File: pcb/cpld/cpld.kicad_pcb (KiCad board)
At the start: 4 copper layers, 104.4 x 82.7 mm, 30 parts, among them J1 Micro_SD_Card_Det1, J2 Bus_ISA_8bit_AB_Rev0, J3 Atmel-JTAG-10, SW1 ADDR SEL, U1 ATF1504AS-xJx44, U2 AMS1117-3.3, U3 74LVC125, U4 74HCT688, X1 16MHz

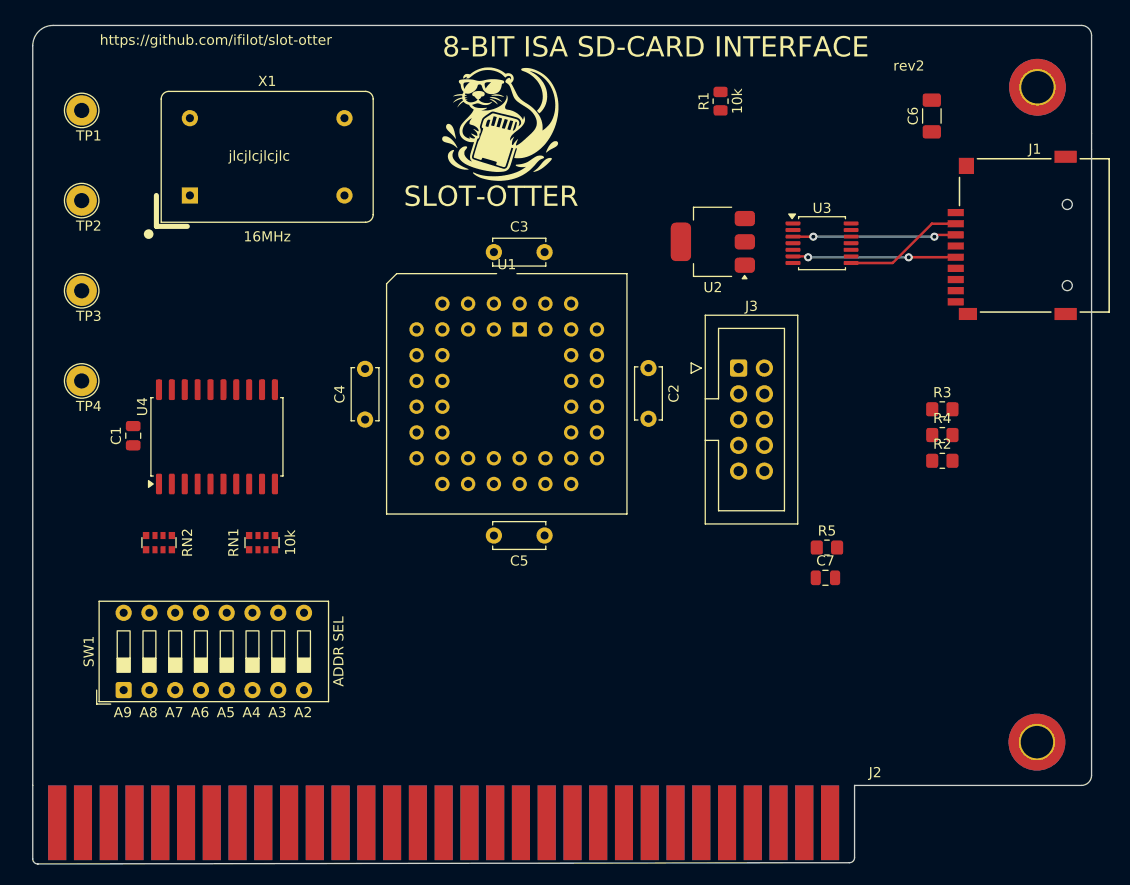
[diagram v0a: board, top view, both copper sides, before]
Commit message: Refactoring otternav and initial commit copying from HD to SD
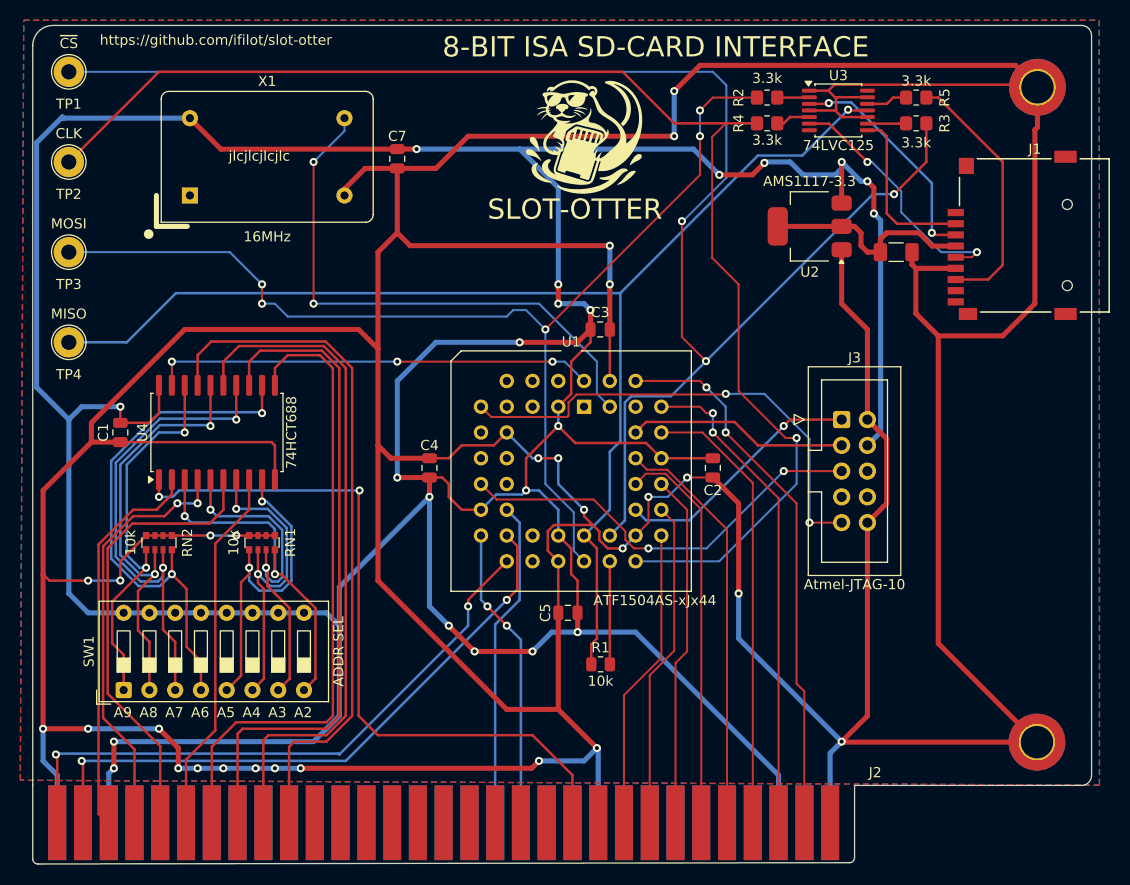
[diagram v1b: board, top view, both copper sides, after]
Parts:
- C2, C3, C4, C5: footprint Capacitor_THT:C_Disc_D5.0mm_W2.5mm_P5.00mm -> Capacitor_SMD:C_0805_2012Metric
- moved C7 59.1 mm to (112.6, 50.7), turned to -90 degrees
- moved R1 56.8 mm to (132.7, 100.6), turned to 0 degrees
- moved R5 45.2 mm to (163.8, 44.7), turned to 180 degrees
- moved R2 39.8 mm to (149.1, 44.7)
- moved R4 35.3 mm to (149.1, 47.2)
- moved R3 28.3 mm to (163.8, 47.2), turned to 180 degrees
- moved C6 13.9 mm to (161.8, 59.9), turned to 0 degrees
- moved U3 13.2 mm to (156.1, 46.0)
- moved C3 13.0 mm to (132.6, 67.5)
- moved C2 11.7 mm to (143.7, 81.2)
- moved J3 11.4 mm to (156.4, 76.4)
- moved U1 9.92 mm to (131.0, 75.2)
- moved U2 9.67 mm to (153.3, 57.4)
- moved G*** 8.35 mm to (131.0, 48.5)
- moved C5 7.96 mm to (129.5, 95.5)
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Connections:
- SW1 pad 5: Net-(RN1A-R1.2) -> Net-(RN1D-R4.2)
- SW1 pad 6: Net-(RN1B-R2.2) -> Net-(RN1C-R3.2)
- SW1 pad 7: Net-(RN1C-R3.2) -> Net-(RN1B-R2.2)
- SW1 pad 8: Net-(RN1D-R4.2) -> Net-(RN1A-R1.2)
- U1 pad 11: DB5 -> unconnected-(U1-I/O/PD1-Pad11)
- U1 pad 12: DB6 -> unconnected-(U1-I/O-Pad12)
- U1 pad 14: DB7 -> unconnected-(U1-I/O-Pad14)
- U1 pad 15: +5V -> VCC
- U1 pad 23: +5V -> VCC
- U1 pad 29: unconnected-(U1-I/O-Pad29) -> DB0
- U1 pad 3: +5V -> VCC
- U1 pad 31: unconnected-(U1-I/O-Pad31) -> DB1
- U1 pad 33: unconnected-(U1-I/O-Pad33) -> DB2
- U1 pad 34: unconnected-(U1-I/O-Pad34) -> DB3
- U1 pad 35: +5V -> VCC
- U1 pad 36: unconnected-(U1-I/O-Pad36) -> DB4
- U1 pad 37: unconnected-(U1-I/O-Pad37) -> DB5
- U1 pad 39: unconnected-(U1-I/O-Pad39) -> DB6
- U1 pad 4: DB0 -> unconnected-(U1-I/O-Pad4)
- U1 pad 40: unconnected-(U1-I/O-Pad40) -> DB7
- U1 pad 5: DB1 -> unconnected-(U1-I/O-Pad5)
- U1 pad 6: DB2 -> unconnected-(U1-I/O-Pad6)
- U1 pad 8: DB3 -> unconnected-(U1-I/O-Pad8)
- U1 pad 9: DB4 -> unconnected-(U1-I/O-Pad9)
- U4 pad 3: Net-(RN1D-R4.2) -> Net-(RN1A-R1.2)
- U4 pad 5: Net-(RN1C-R3.2) -> Net-(RN1B-R2.2)
- U4 pad 7: Net-(RN1B-R2.2) -> Net-(RN1C-R3.2)
- U4 pad 9: Net-(RN1A-R1.2) -> Net-(RN1D-R4.2)
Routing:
- net GND: track 0.00 -> 674.7 mm, vias 0 -> 27
- net VCC: track 0.00 -> 444.7 mm, vias 0 -> 21
- net ~{CS}: track 0.00 -> 152.5 mm, vias 0 -> 3
- net CLK: track 0.00 -> 132.9 mm, vias 0 -> 1
- net MISO: track 0.00 -> 127.1 mm, vias 0 -> 1
- net MOSI: track 0.00 -> 110.3 mm, vias 0 -> 5
- net AEN: track 0.00 -> 72.3 mm, vias 0 -> 2
- net A9: track 0.00 -> 69.3 mm
- net A8: track 0.00 -> 67.6 mm
- net A7: track 0.00 -> 66.3 mm
- net A6: track 0.00 -> 63.6 mm
- net A1: track 0.00 -> 62.0 mm, vias 0 -> 2
- net A0: track 0.00 -> 60.8 mm, vias 0 -> 2
- net 16MHz: track 0.00 -> 54.8 mm, vias 0 -> 2
- net DB7: track 0.00 -> 54.3 mm, vias 0 -> 2
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- added copper zone on F.Cu, net GND
- added copper zone on B.Cu, net VCC
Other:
- copper layers 4 -> 2
- board text removed: "rev2"

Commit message: Refining CPLD card
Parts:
- added TP5: GND, TestPoint:TestPoint_Loop_D2.54mm_Drill1.5mm_Beaded, F.Cu at (92.2, 40.2)
- added TP6: GND, TestPoint:TestPoint_Loop_D2.54mm_Drill1.5mm_Beaded, F.Cu at (107.4, 40.1)
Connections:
- U3 pad 14: (no net) -> +3V3
- U3 pad 7: (no net) -> GND
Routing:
- net +3V3: track 21.4 -> 44.4 mm, vias 0 -> 2
- net GND: track 674.7 -> 690.0 mm, vias 27 -> 29
- net ~{CS}: track 152.5 -> 163.0 mm
- net CLK: track 132.9 -> 131.6 mm
